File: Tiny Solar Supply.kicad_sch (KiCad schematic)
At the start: 14 parts, among them J1 Conn_01x02_Pin, J2 Conn_01x02_Pin, J3 Conn_01x02_Pin, J4 Conn_01x02_Pin, Q1 2N7002, U1 SS14, U2 SS14

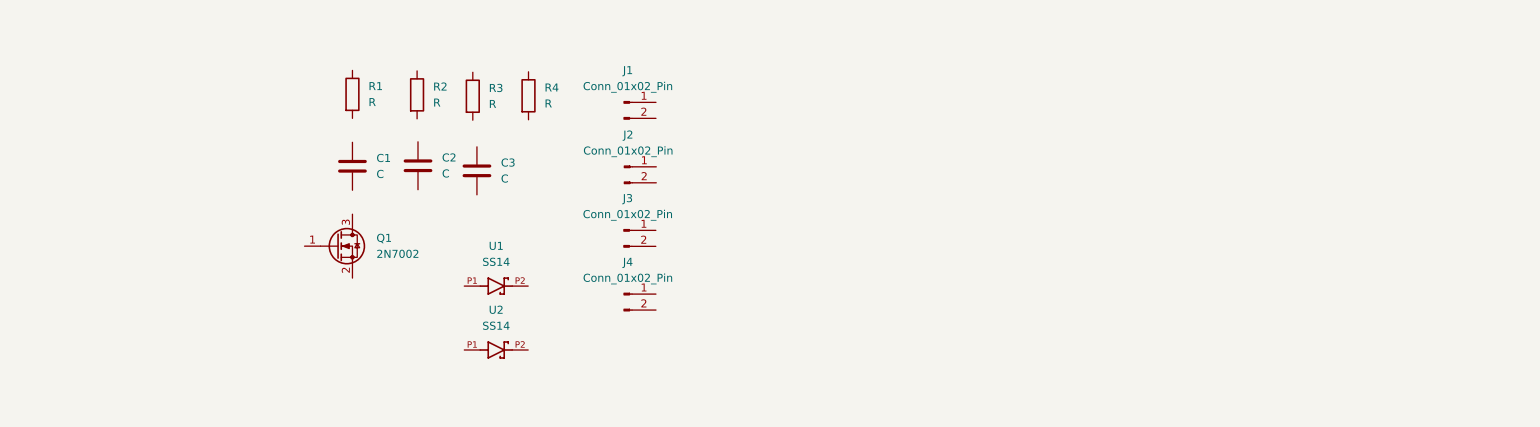
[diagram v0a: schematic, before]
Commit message: Footprints and symbol arranged
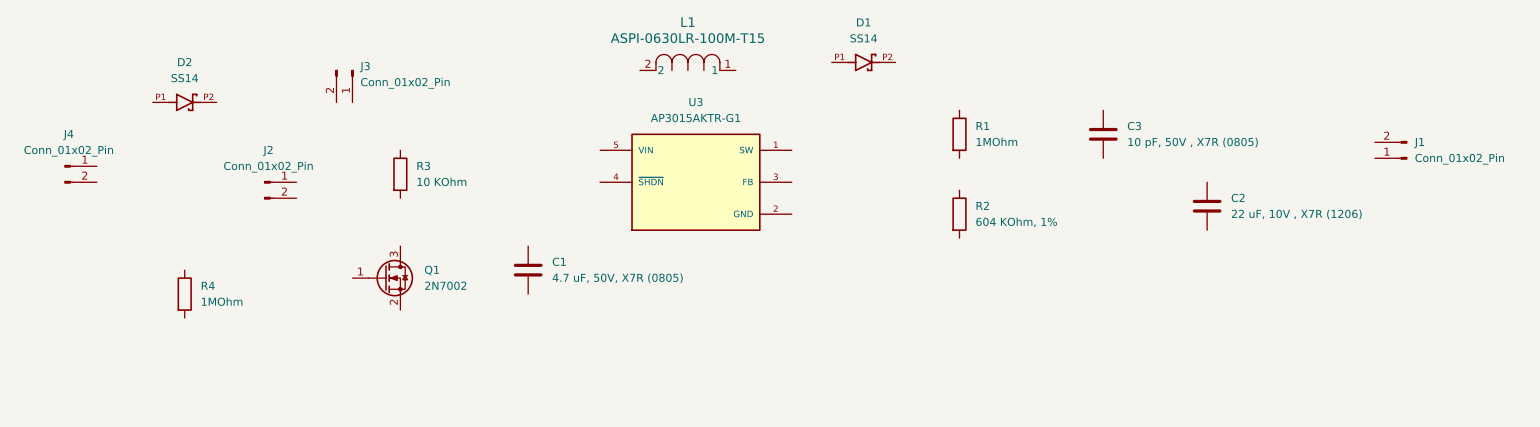
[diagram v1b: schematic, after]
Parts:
- added L1: ASPI-0630LR-100M-T15, Schotty:IND_ASPI-0630LR_ABR, symbol Schotty IND_ASPI-0630LR_ABR:ASPI-0630LR-100M-T15
- added U3: AP3015AKTR-G1, AP3015AKTR-G1:SOT95P280X145-5N, symbol AP3015AKTR-G1:AP3015AKTR-G1
- C1: value C -> 4.7 uF, 50V, X7R (0805); footprint (none) -> Capacitor_SMD:C_0805_2012Metric
- C2: value C -> 22 uF, 10V , X7R (1206); footprint (none) -> Capacitor_SMD:C_1206_3216Metric
- C3: value C -> 10 pF, 50V , X7R (0805); footprint (none) -> Capacitor_SMD:C_0805_2012Metric
- J1, J2, J3: footprint Package_TO_SOT_SMD:SOT-23 -> Connector_PinHeader_2.54mm:PinHeader_1x02_P2.54mm_Vertical
- J4: footprint Package_TO_SOT_SMD:SOT-23 -> Connector_PinHeader_2.54mm:PinHeader_1x02_P2.54mm_Horizontal
- R1, R4: value R -> 1MOhm; footprint (none) -> Resistor_SMD:R_0805_2012Metric
- R2: value R -> 604 KOhm, 1%; footprint (none) -> Resistor_SMD:R_0805_2012Metric
- R3: value R -> 10 KOhm; footprint (none) -> Resistor_SMD:R_0805_2012Metric
- renumbered U1 to D1, U2 to D2
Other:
- moved on the sheet: C1, C2, C3, D1, D2, J1, J2, J3, J4, Q1, R1, R2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

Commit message: Schematic design done
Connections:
- net at R2.1: now also C3.2, R1.2, U3.3 (FB)
- net GND: now reaches R2.2
- net GND: now also C1.2, C2.2, J1.1 (Pin_1), J2.2 (Pin_2), J4.2 (Pin_2), Q1.2 (S), R4.2, U3.2 (GND)
- net at C1.1: now also J3.1 (Pin_1), L1.2, R3.1, U3.5 (VIN)
- net SOLAR_P: now reaches D2.P1
- net SOLAR_P: now also J4.1 (Pin_1), Q1.1 (G), R4.1
- net BAT_P: now reaches D2.P2
- net BAT_P: now also J2.1 (Pin_1), J3.2 (Pin_2)
- net at L1.1: now also D1.P1, U3.1 (SW)
- net OUT_P: now reaches D1.P2
- net OUT_P: now also C2.1, C3.1, J1.2 (Pin_2), R1.1
- net at Q1.3 (D): now also R3.2, U3.4 (~{SHDN})
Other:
- moved on the sheet: C1, C2, C3, D1, J1, J2, J3, L1, R1, R2, R3, R4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
